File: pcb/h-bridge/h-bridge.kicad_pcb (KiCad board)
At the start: 2 copper layers, 110 x 70 mm, 66 parts, among them J1 B2B-XH-A, J2 S2B-XH-A, J3 S2B-XH-A, J5 B5B-XH-A, U1 MCT6, U10 IRFZ44, U11 IRFZ44, U12 IRFZ44, U13 IRFZ44, U14 IRFZ44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

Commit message: pcbs reviewed
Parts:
- moved J1 2.50 mm to (184.4, 98.2)
- moved C5 2.49 mm to (176.4, 98.9), turned to 0 degrees
- moved G*** 1.50 mm to (119.5, 68.3)
- moved G*** 1.50 mm to (114.7, 68.1)
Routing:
- net /GATE3: track 42.5 -> 91.3 mm
- net /GATE2: track 41.6 -> 85.3 mm, vias 0 -> 1
- net +16V: track 223.5 -> 226.9 mm
- net /GATE1: track 27.5 -> 28.7 mm
- net /MOTOR-_2: track 23.2 -> 22.4 mm
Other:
- board text added: "H-Bridge V1.0 ENPH 253 2025 Team 4 - Hot Dawgs"
- board text removed: "H-Bridge V1.0 ENPH 253 2025 Team 4"

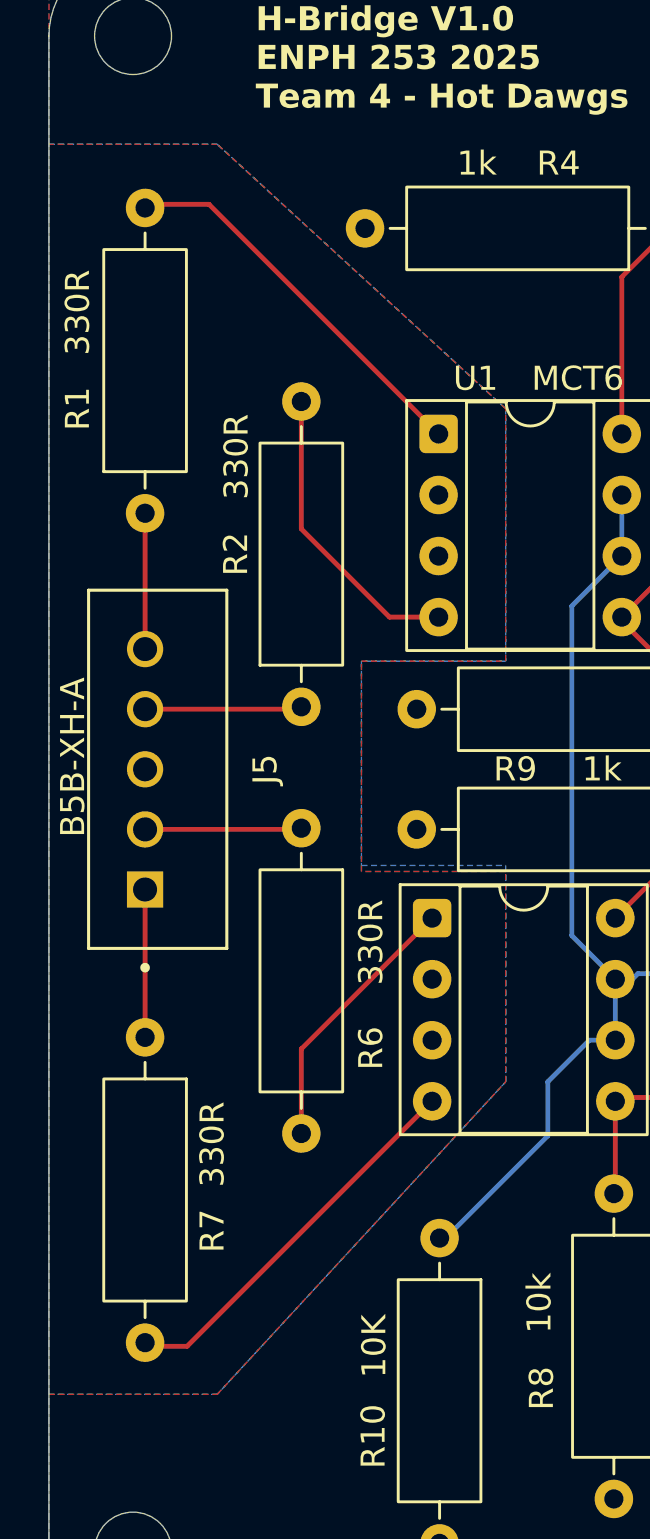
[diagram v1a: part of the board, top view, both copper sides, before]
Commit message: expanded h-bridge ground plane
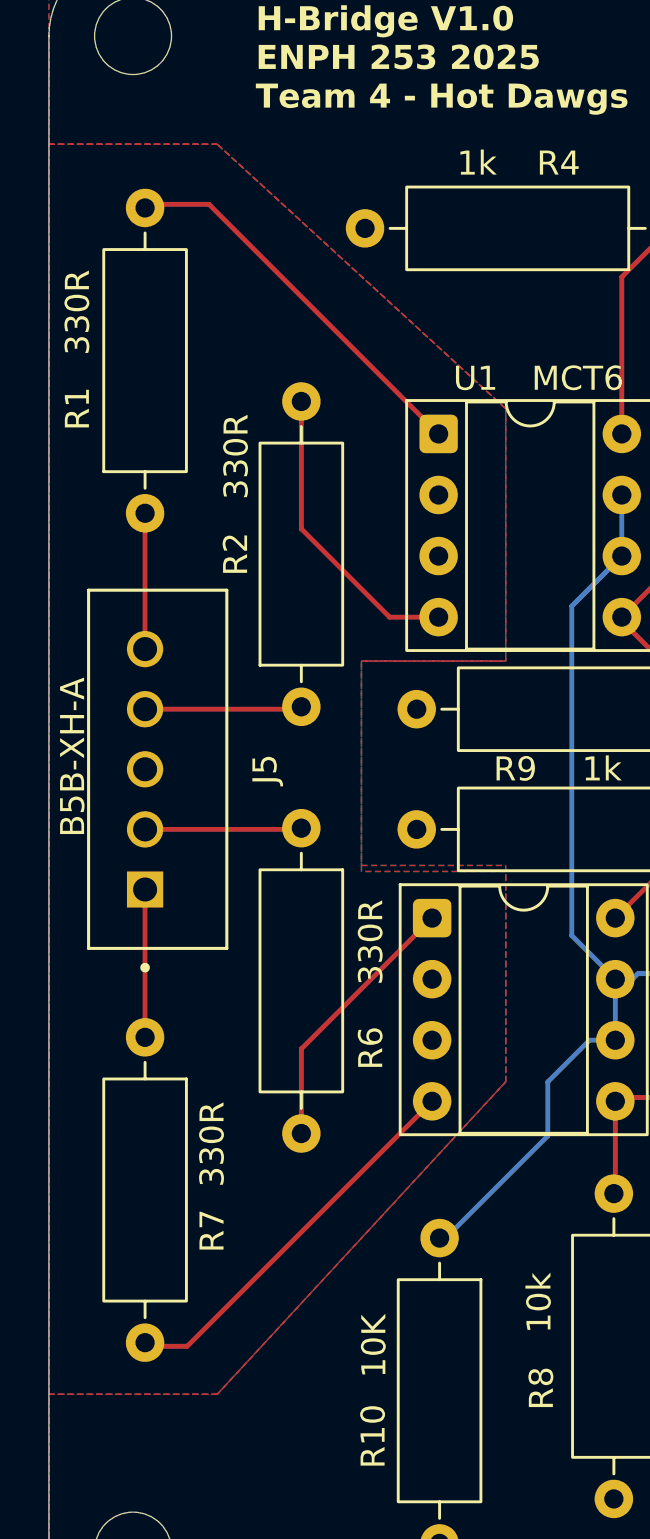
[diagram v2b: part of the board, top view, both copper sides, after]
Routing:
- added copper zone on F.Cu, net ESP_GND
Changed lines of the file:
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@@
+	)
+	(zone
+		(net 39)
+		(net_name "ESP_GND")
+		(layers "F.Cu" "B.Cu")
+		(name "ESP_GND")
+		(hatch edge 0.5)
+		(connect_pads
+			(clearance 0.5)
+		)
+		(min_thickness 0.25)
+		(filled_areas_thickness no)
+		(fill yes
+			(thermal_gap 0.5)
+			(thermal_bridge_width 0.5)
+		)
+		(polygon
+			(pts
+				(xy 87.95 71.9) (xy 94.95 71.9) (xy 106.95 82.9) (xy 106.95 93.4) (xy 100.95 93.4) (xy 100.95 101.9)
+				(xy 106.95 101.9) (xy 106.95 110.9) (xy 94.95 123.9) (xy 87.95 123.9)
+			)
+		)
 	)
 	(zone
@@
 			)
 		)
-	)
-	(zone
-		(net 39)
-		(net_name "ESP_GND")
-		(layer "B.Cu")
-		(name "ESP_GND")
-		(hatch edge 0.5)
-		(connect_pads
-			(clearance 0.5)
-		)
-		(min_thickness 0.25)
-		(filled_areas_thickness no)
-		(fill yes
-			(thermal_gap 0.5)
-			(thermal_bridge_width 0.5)
-		)
-		(polygon
-			(pts
-				(xy 87.95 71.9) (xy 94.95 71.9) (xy 106.95 82.9) (xy 106.95 93.4) (xy 100.95 93.4) (xy 100.95 101.9)
-				(xy 106.95 101.9) (xy 106.95 110.9) (xy 94.95 123.9) (xy 87.95 123.9)
-			)
-		)
